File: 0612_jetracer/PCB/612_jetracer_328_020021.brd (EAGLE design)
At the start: 84.4 x 80 mm, 133 parts, among them IC2 JETSON_NANO_NOBORDER, IC3 MULTIPLEXERSMC74HC157A, IC4 PCA9685_BOTTOM, M1 MOSFET-N_FDV301N, M4 MOSFET-N_FDV301N, T10 T2N7002AK, T11 T2N7002AK, U12 SSM6N7002KFU, U20 SN74LVC1G17, U21 SSM6N7002KFU, U23 SN74LVC1G17, U3 TLP291A, U5 TLP2270, U7 TLP291A, X2 16MHz

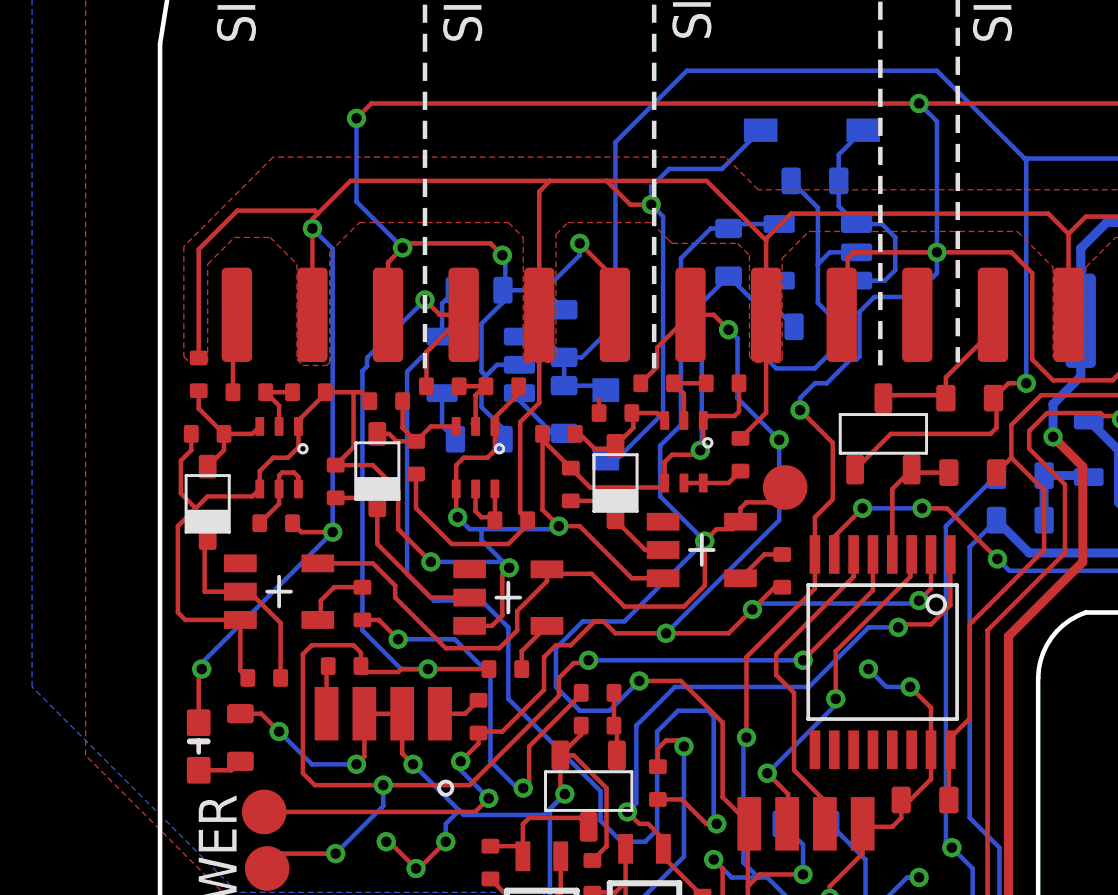
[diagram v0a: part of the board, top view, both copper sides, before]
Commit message: #612 JetRacer Rev2.0.21配線修正
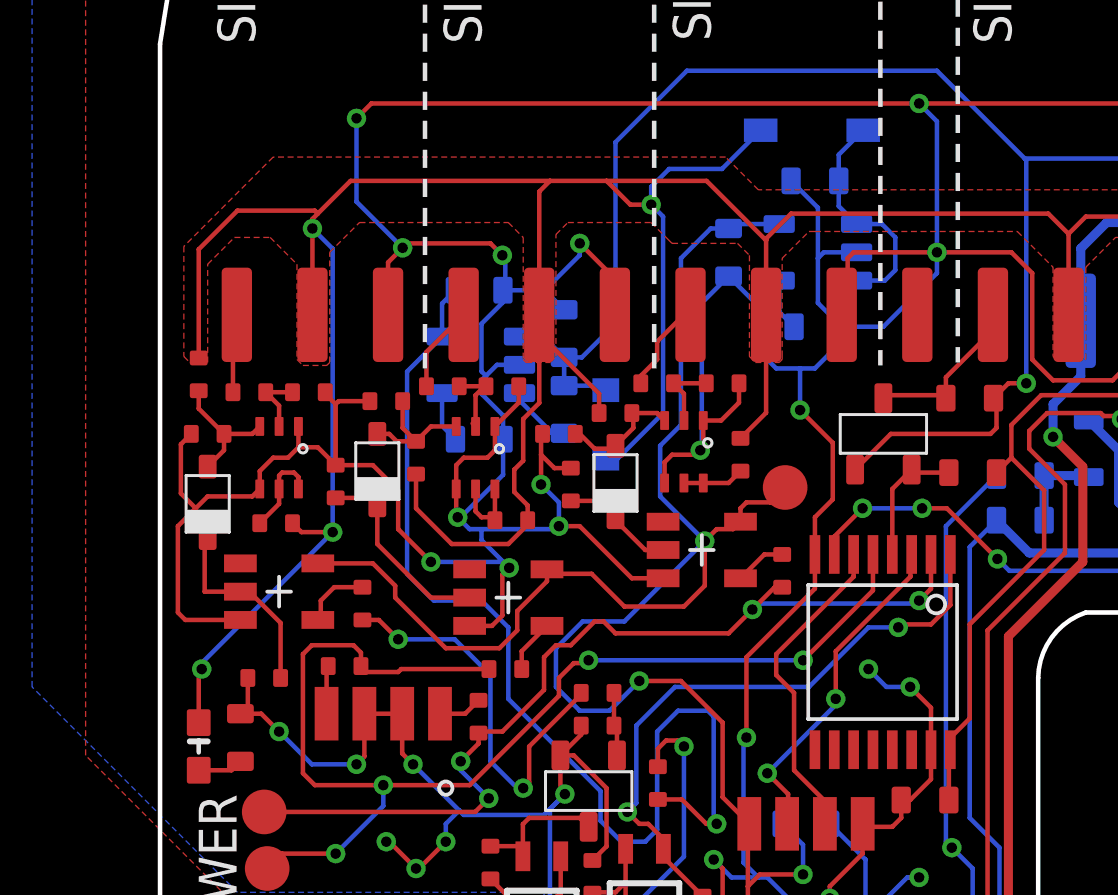
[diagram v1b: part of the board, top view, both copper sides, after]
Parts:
- R11, R14: value 1K -> 330
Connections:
- net PCH_3 renamed SIGNAL3_INPUT
- removed net RC_GND: C11.1, C13.1, C16.1, IC7.2, R64.1, R65.1, R66.1, R67.1, R68.1, R69.1, R70.1, R71.1, R72.1, U$10.1, U$10.4, U$7.3, U12.1, U12.4, U20.3, U21.1, U21.4, U23.3
- new net SIGNAL1_INPUT: R61.1, U$1.7:SIGNAL1
- new net SIGNAL2_INPUT: R62.1, U$1.4:SIGNAL2
- net 0: now also C11.1, C13.1, C16.1, IC7.2, R64.1, R65.1, R66.1, R67.1, R68.1, R69.1, R70.1, R71.1, R72.1, U$10.1, U$10.4, U$7.3, U12.1, U12.4, U20.3, U21.1, U21.4, U23.3
- net PCH1: no longer R61.1, U$1.7:SIGNAL1
- net PCH2: no longer R62.1, U$1.4:SIGNAL2
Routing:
- net RC_GND: track 82.2 -> 0.00 mm, vias 5 -> 0
- net 0: track 230.2 -> 308.3 mm, vias 33 -> 39
- net PCH2: track 59.5 -> 40.3 mm, vias 6 -> 4
- net PCH1: track 48.2 -> 31.2 mm, vias 7 -> 4
- net RC_VCC: track 116.8 -> 120.0 mm
- net SIGNAL1_INPUT: track 0.00 -> 3.12 mm
- net SIGNAL2_INPUT: track 0.00 -> 2.92 mm
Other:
- board text added: "#612 JetRacer Rev 2.0.21 B 2022/06/04"
- board text added: "2C3325-Y"
- board text added: "AVR 328P"
- board text added: "F-612-2-21-A-N-J-2-P"
- board text added: "ID2"
- board text added: "MC74HC157A"
- board text added: "S/N"
- board text added: "TLP2270"
- board text removed: "#612 JetRacer Rev 2.0.21 2022/04/19"
- board text removed: "F-612-2-21-A-N-J-1-P"

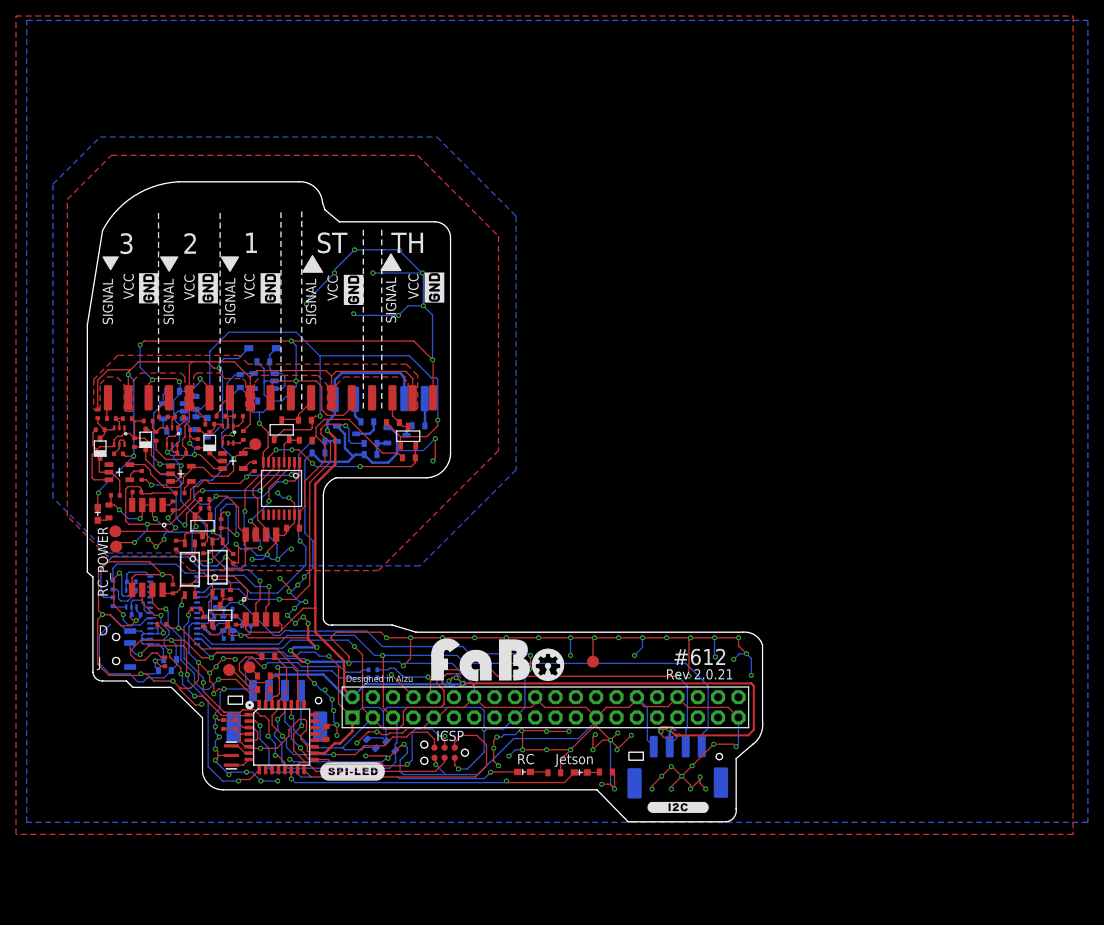
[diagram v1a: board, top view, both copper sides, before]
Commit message: #612 JetRacer 出力インピーダンス改善、I 2C表記大きく
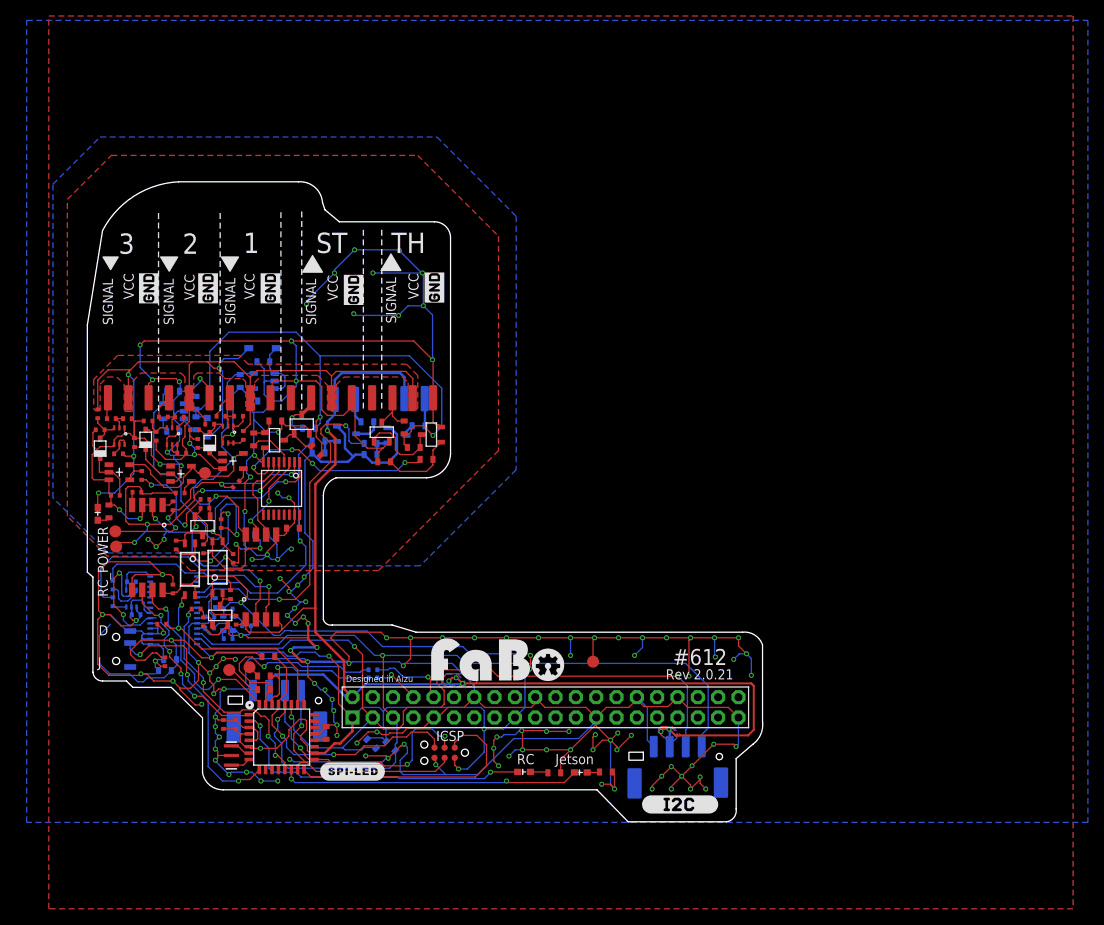
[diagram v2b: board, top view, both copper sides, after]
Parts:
- added R20, R48: 1K, FaBo-Resistors:0603
- added R21: 330, FaBo-Resistors:0603
- added R47: 100, FaBo-Resistors:0603
- added T3, T4: T2N7002AK, FaBo-Mosfet:SOT-23
- added U$14: (no value), FaBo-Logo:LOGO_SILK_I2C
- R11: value 330 -> 1K
- R18: value DNP -> 100
- R19: value DNP -> 1K
- moved R19 17.3 mm to (23.5, 50.1)
- moved R14 10.5 mm to (27.7, 49.2), flipped to the bottom
- moved TP4 7.26 mm to (14.7, 43.6)
- moved R18 6.50 mm to (20.8, 47.8), turned to 90 degrees
- moved R11 4.05 mm to (28.6, 46.4), turned to 135 degrees
- moved R7 3.18 mm to (18.6, 42.2), turned to 45 degrees
- moved T11 2.91 mm to (43.0, 48.4), turned to 90 degrees
- moved T10 1.58 mm to (23.4, 47.7), turned to 270 degrees
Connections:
- new net N$18: R11.2, T10.3, T3.1
- new net N$35: R18.2, R19.1, T10.1
- new net N$36: R20.2, T11.3, T4.1
- new net RC_VCC2: C21.2, D2.C, IC5.1, R11.1, R14.1, R20.1, R21.1, R31.1
- net 0: now also R19.2, R48.2, T10.2, T11.2, T3.2, T4.2
- net N$3: no longer R18.1, R19.1
- net N$34: now also R47.2, R48.1; no longer C21.2, D2.C, IC5.1, R11.1, R14.1, R31.1, T10.1
- net RCH1: now also R18.1; no longer R18.2, T10.2
- net RCH2: now also R47.1; no longer R19.2, T11.2
- net ST_OUTPUT: now also R14.2, T3.3; no longer R11.2, T10.3
- net TH_OUTPUT: now also R21.2, T4.3; no longer R14.2, T11.3
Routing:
- net RC_VCC2: track 0.00 -> 73.0 mm, vias 0 -> 2
- net N$34: track 74.4 -> 9.39 mm, vias 2 -> 0
- net 0: track 308.3 -> 338.8 mm, vias 39 -> 41
- net N$3: track 28.3 -> 2.11 mm
- net N$36: track 0.00 -> 10.5 mm
- net GND: track 574.1 -> 565.7 mm, vias 106 -> 104
- net RCH2: track 22.5 -> 28.3 mm
- net N$18: track 0.00 -> 4.45 mm
- net N$35: track 0.00 -> 3.08 mm
- net RC_+B_3V3: track 70.6 -> 68.4 mm
- net RCH1: track 4.45 -> 5.70 mm
- net RC_VCC: track 120.0 -> 121.2 mm
- net TH_OUTPUT: track 4.76 -> 5.88 mm
- net ST_OUTPUT: track 5.60 -> 6.32 mm, vias 0 -> 1
- net N$14: track 10.8 -> 11.3 mm
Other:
- board text added: "#612 JetRacer Rev 2.0.21 B 2022/06/06"
- board text added: "2N7002K"
- board text removed: "#612 JetRacer Rev 2.0.21 B 2022/06/04"

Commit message: R28 104から472に抵抗を変更。
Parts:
- R28: value 10K/0402 -> 4.7K/0402
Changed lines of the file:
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@@
 <drawing>
 <settings>
-<setting alwaysvectorfont="yes"/>
+<setting alwaysvectorfont="no"/>
 <setting keepoldvectorfont="yes"/>
 <setting verticaltext="up"/>
@@
 <attribute name="VALUE" x="11" y="34.8" size="0.4064" layer="51" font="vector" ratio="12" rot="R90" align="center"/>
 </element>
-<element name="R28" library="FaBo-Resistors" package="0402" value="10K/0402" x="14.7" y="40.3" smashed="yes" rot="R180">
+<element name="R28" library="FaBo-Resistors" package="0402" value="4.7K/0402" x="14.7" y="40.3" smashed="yes" rot="R180">
 <attribute name="VALUE" x="14.7" y="39.9" size="0.4064" layer="51" font="vector" ratio="12" rot="R180" align="center"/>
 </element>

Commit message: #612 JetRacer Rev2.0.21 10K->0に変更。
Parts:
- R3: value 10K/0402 -> 0/0402
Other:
- board text added: "#612 JetRacer Rev 2.0.21 B 2022/06/06 2022/09/15 R3 10K->0"
- board text removed: "#612 JetRacer Rev 2.0.21 B 2022/06/06"
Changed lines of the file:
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@@
 <text x="72.5" y="20.5" size="1.27" layer="22" font="vector" ratio="10" rot="MR0">Rev 2.0.21</text>
 <text x="55.2" y="-8.3" size="1.27" layer="48" font="vector" ratio="14">#612 JetRacer Rev 2.0.21 B
-2022/06/06</text>
+2022/06/06
+2022/09/15 R3 10K-&gt;0</text>
 <wire x1="10.5" y1="16.8" x2="14.4" y2="13" width="0.1524" layer="20"/>
 <wire x1="14.4" y1="13" x2="14.4" y2="6.1" width="0.1524" layer="20"/>
@@
 <attribute name="VALUE" x="15.225" y="23.72" size="0.254" layer="52" font="vector" ratio="12" rot="MR0" align="center"/>
 </element>
-<element name="R3" library="FaBo-Resistors" package="0402" value="10K/0402" x="15.325" y="25.62" smashed="yes" rot="MR0">
+<element name="R3" library="FaBo-Resistors" package="0402" value="0/0402" x="15.325" y="25.62" smashed="yes" rot="MR0">
 <attribute name="VALUE" x="15.375" y="25.22" size="0.254" layer="52" font="vector" ratio="12" rot="MR0" align="center"/>
 </element>

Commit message: #612 JetRacer定数変更 R1 10K->0
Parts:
- R1: value 10K/0402 -> 0/0402
- R3: value 0/0402 -> 10K/0402
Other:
- board text added: "#612 JetRacer Rev 2.0.21 B 2022/06/06 2022/09/16 R1 10K->0"
- board text removed: "#612 JetRacer Rev 2.0.21 B 2022/06/06 2022/09/15 R3 10K->0"
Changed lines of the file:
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@@
 <text x="55.2" y="-8.3" size="1.27" layer="48" font="vector" ratio="14">#612 JetRacer Rev 2.0.21 B
 2022/06/06
-2022/09/15 R3 10K-&gt;0</text>
+2022/09/16 R1 10K-&gt;0</text>
 <wire x1="10.5" y1="16.8" x2="14.4" y2="13" width="0.1524" layer="20"/>
 <wire x1="14.4" y1="13" x2="14.4" y2="6.1" width="0.1524" layer="20"/>
@@
 <attribute name="VALUE" x="18.625" y="32.97" size="0.4064" layer="51" font="vector" ratio="12" rot="R90" align="center"/>
 </element>
-<element name="R1" library="FaBo-Resistors" package="0402" value="10K/0402" x="15.275" y="24.22" smashed="yes" rot="MR0">
+<element name="R1" library="FaBo-Resistors" package="0402" value="0/0402" x="15.275" y="24.22" smashed="yes" rot="MR0">
 <attribute name="VALUE" x="15.225" y="23.72" size="0.254" layer="52" font="vector" ratio="12" rot="MR0" align="center"/>
 </element>
-<element name="R3" library="FaBo-Resistors" package="0402" value="0/0402" x="15.325" y="25.62" smashed="yes" rot="MR0">
+<element name="R3" library="FaBo-Resistors" package="0402" value="10K/0402" x="15.325" y="25.62" smashed="yes" rot="MR0">
 <attribute name="VALUE" x="15.375" y="25.22" size="0.254" layer="52" font="vector" ratio="12" rot="MR0" align="center"/>
 </element>

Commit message: #612 JetRacer Rev2.0.21 実装部品の注釈追加。
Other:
- board text added: "#612 JetRacer Rev 2.0.21 B 2022/06/06 2022/09/16 R1 10K->0 2022/09/29 2SC3325->2SC2712"
- board text added: "1N4148WS"
- board text added: "2SC2712"
- board text added: "LP2985-33"
- board text added: "LP2985-50"
- board text removed: "#612 JetRacer Rev 2.0.21 B 2022/06/06 2022/09/16 R1 10K->0"
- board text removed: "2C3325-Y"
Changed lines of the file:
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@@
 <text x="55.2" y="-8.3" size="1.27" layer="48" font="vector" ratio="14">#612 JetRacer Rev 2.0.21 B
 2022/06/06
-2022/09/16 R1 10K-&gt;0</text>
+2022/09/16 R1 10K-&gt;0
+2022/09/29 2SC3325-&gt;2SC2712</text>
 <wire x1="10.5" y1="16.8" x2="14.4" y2="13" width="0.1524" layer="20"/>
 <wire x1="14.4" y1="13" x2="14.4" y2="6.1" width="0.1524" layer="20"/>
@@
 <text x="78.7" y="21.8" size="1.27" layer="22" font="vector" ratio="18" rot="MR180">ID2</text>
 <text x="20.9" y="71.4" size="1.5" layer="22" font="vector" ratio="18" rot="MR180">S/N</text>
-<text x="15.4" y="26" size="0.4064" layer="48" font="vector" ratio="15">2C3325-Y</text>
-<text x="13.7" y="37.1" size="0.4064" layer="48" font="vector" ratio="15">2C3325-Y</text>
 <text x="42.6" y="48.1" size="0.3048" layer="48" font="vector" ratio="15">2N7002K</text>
 <text x="35.8" y="48.7" size="0.3048" layer="48" font="vector" ratio="15">2N7002K</text>
 <text x="26.1" y="49.8" size="0.3048" layer="48" font="vector" ratio="15">2N7002K</text>
 <text x="22.4" y="47.8" size="0.3048" layer="48" font="vector" ratio="15">2N7002K</text>
+<text x="25.4" y="54.6" size="0.8" layer="52" font="vector" rot="MR0">LP2985-33</text>
+<text x="13.4" y="51.5" size="0.8" layer="52" font="vector" rot="MR0">LP2985-50</text>
+<text x="13.1" y="36.5" size="0.4" layer="51" font="vector" ratio="15">2SC2712</text>
+<text x="15.3" y="25.7" size="0.4" layer="51" font="vector" ratio="15">2SC2712</text>
+<text x="1.4" y="44.9" size="0.4" layer="51" font="vector" ratio="15" rot="R90">1N4148WS</text>
+<text x="7.8" y="45.9" size="0.4" layer="51" font="vector" ratio="15" rot="R90">1N4148WS</text>
+<text x="15.9" y="45.6" size="0.4" layer="51" font="vector" ratio="15" rot="R90">1N4148WS</text>
 </plain>
 <attributes>
